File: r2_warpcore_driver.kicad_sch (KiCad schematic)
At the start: 1 part, among them U1 ESP32-S3-MINI-1

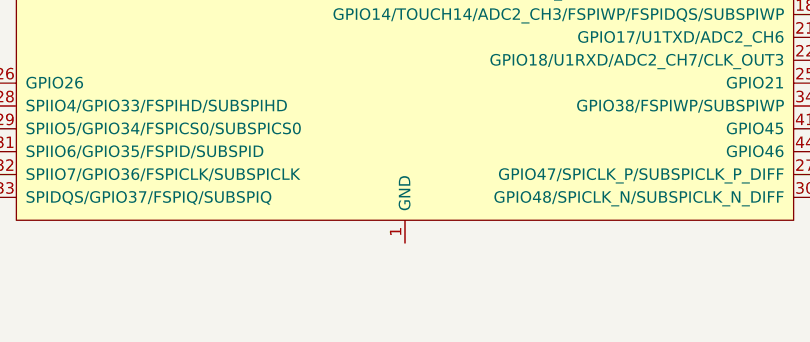
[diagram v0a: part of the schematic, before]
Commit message: Updates to build & adding hash insertion on PCB
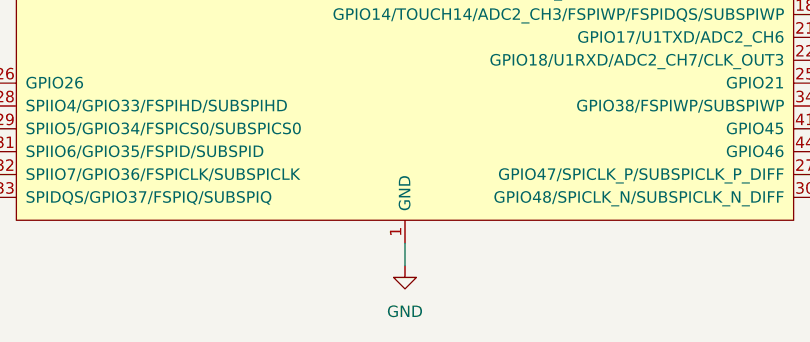
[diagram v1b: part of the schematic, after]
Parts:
- U1: JLCPCB (none) -> C3013941
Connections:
- net GND: now reaches U1.1 (GND), U1.2 (GND), U1.42 (GND), U1.43 (GND), U1.46 (GND), U1.47 (GND), U1.48 (GND), U1.49 (GND), U1.50 (GND), U1.51 (GND), U1.52 (GND), U1.53 (GND), U1.54 (GND), U1.55 (GND), U1.56 (GND), U1.57 (GND), U1.58 (GND), U1.59 (GND), U1.60 (GND), U1.61 (GND), U1.62 (GND), U1.63 (GND), U1.64 (GND), U1.65 (GND)
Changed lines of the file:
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@@
 (kicad_sch (version 20230121) (generator eeschema)
   (paper "A4")
+  (wire (pts (xy 91.44 110.49) (xy 91.44 113.03))
+    (stroke (width 0) (type default))
+  )
   (text "Needs:\n- drive motor control\n- pinout for ESP programming\n- support for pololu regulator to come from 12V down to 5V\n- support for driving 2 servos\n- support for switching on/off laser (7.5 v)\n- support for switching on/off fans (12v)\n- support for RGB LED\n- support for switching on / fog machine (5V 2A?)\n- support for switching on / off strobe (12V)\n- pinout for serial comms?\n- buttons for reset & boot\n- support to read linear actuator position"
     (at 214.63 40.64 0)
     (effects (font (size 1.27 1.27)) (justify left bottom))
+  )
+  (symbol (lib_id "power:GND") (at 91.44 113.03 0) (unit 1)
+    (in_bom yes) (on_board yes) (dnp no) (fields_autoplaced)
+    (property "Reference" "#PWR01" (at 91.44 119.38 0)
+      (effects (font (size 1.27 1.27)) hide)
+    )
+    (property "Value" "GND" (at 91.44 118.11 0)
+      (effects (font (size 1.27 1.27)))
+    )
+    (property "Footprint" "" (at 91.44 113.03 0)
+      (effects (font (size 1.27 1.27)) hide)
+    )
+    (property "Datasheet" "" (at 91.44 113.03 0)
+      (effects (font (size 1.27 1.27)) hide)
+    )
+    (pin "1")
+    (instances
+      (project "r2_warpcore_driver"
+        (path "/6d80d172-24e2-4eb2-ae83-4ad814eadecf"
+          (reference "#PWR01") (unit 1)
+        )
+      )
+    )
   )
   (symbol (lib_id "PCM_Espressif:ESP32-S3-MINI-1") (at 91.44 69.85 0) (unit 1)
@@
       (effects (font (size 1.27 1.27)) hide)
     )
+    (property "JLCPCB" "C3013941" (at 91.44 69.85 0)
+      (effects (font (size 1.27 1.27)) hide)
+    )

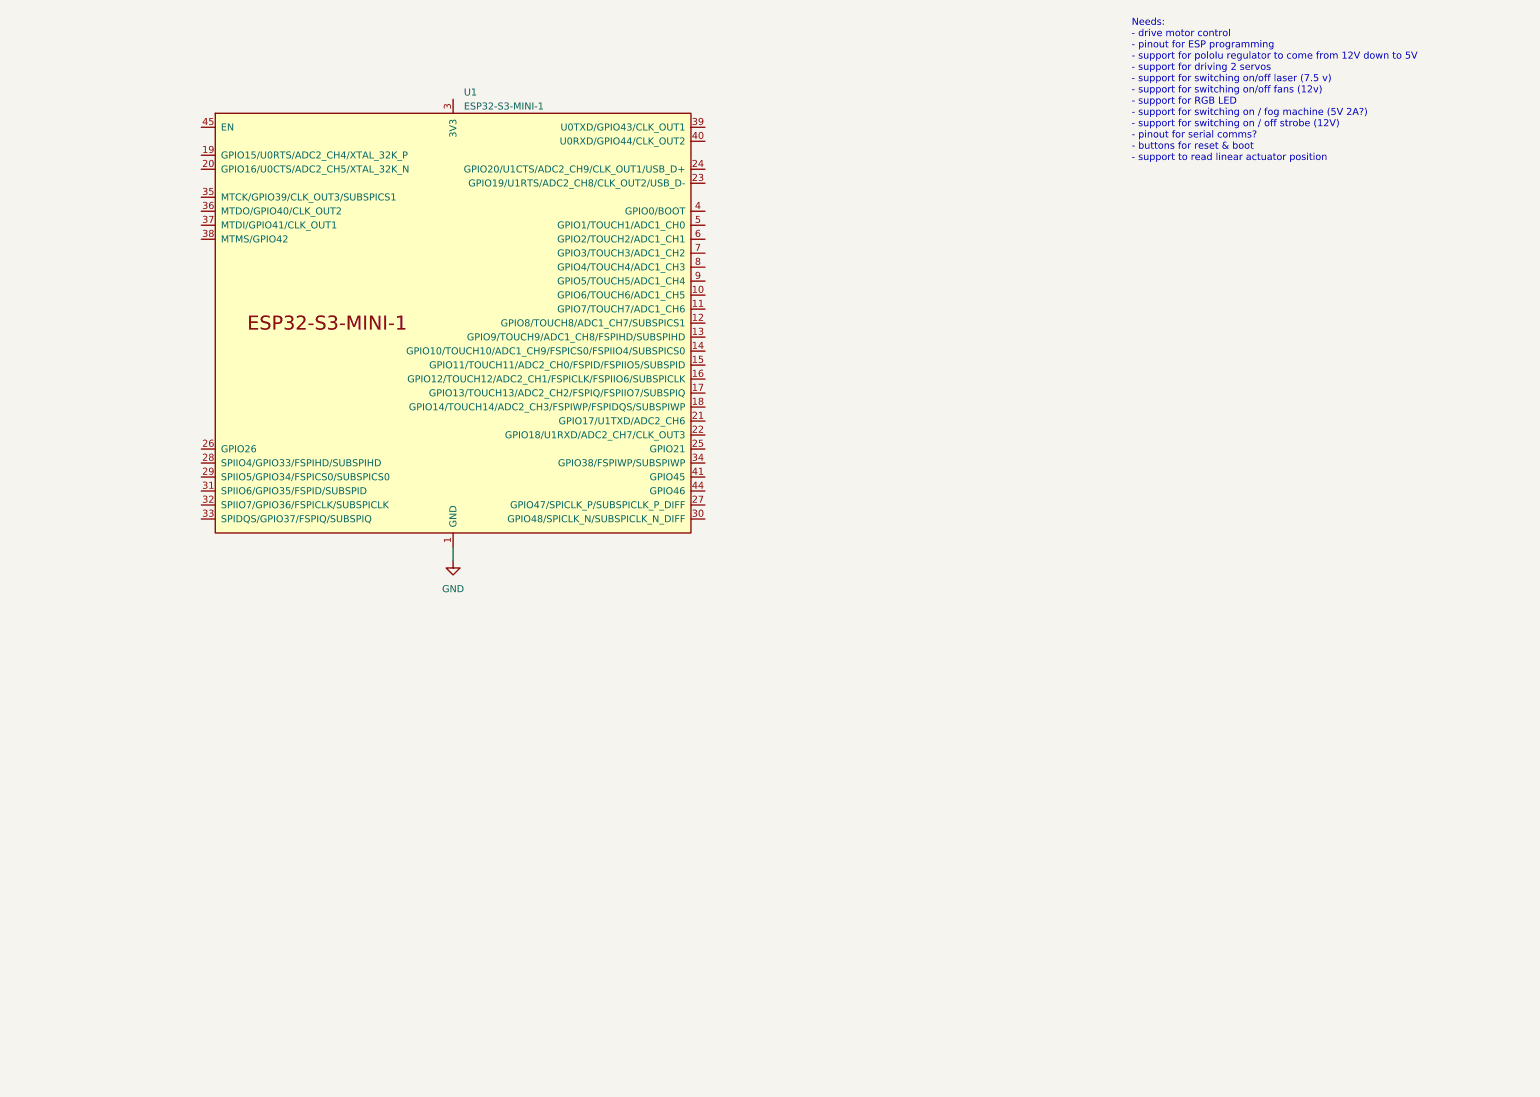
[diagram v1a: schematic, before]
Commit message: Updates with most of the layout completed. Still need to populate some JLCPCB parts and also need to specify the resistors for the LEDS. Should also review if we want to drive the LEDs directly from the MCU or if we want to put in some transistors to drive the LEDs from a higher voltage / current source.
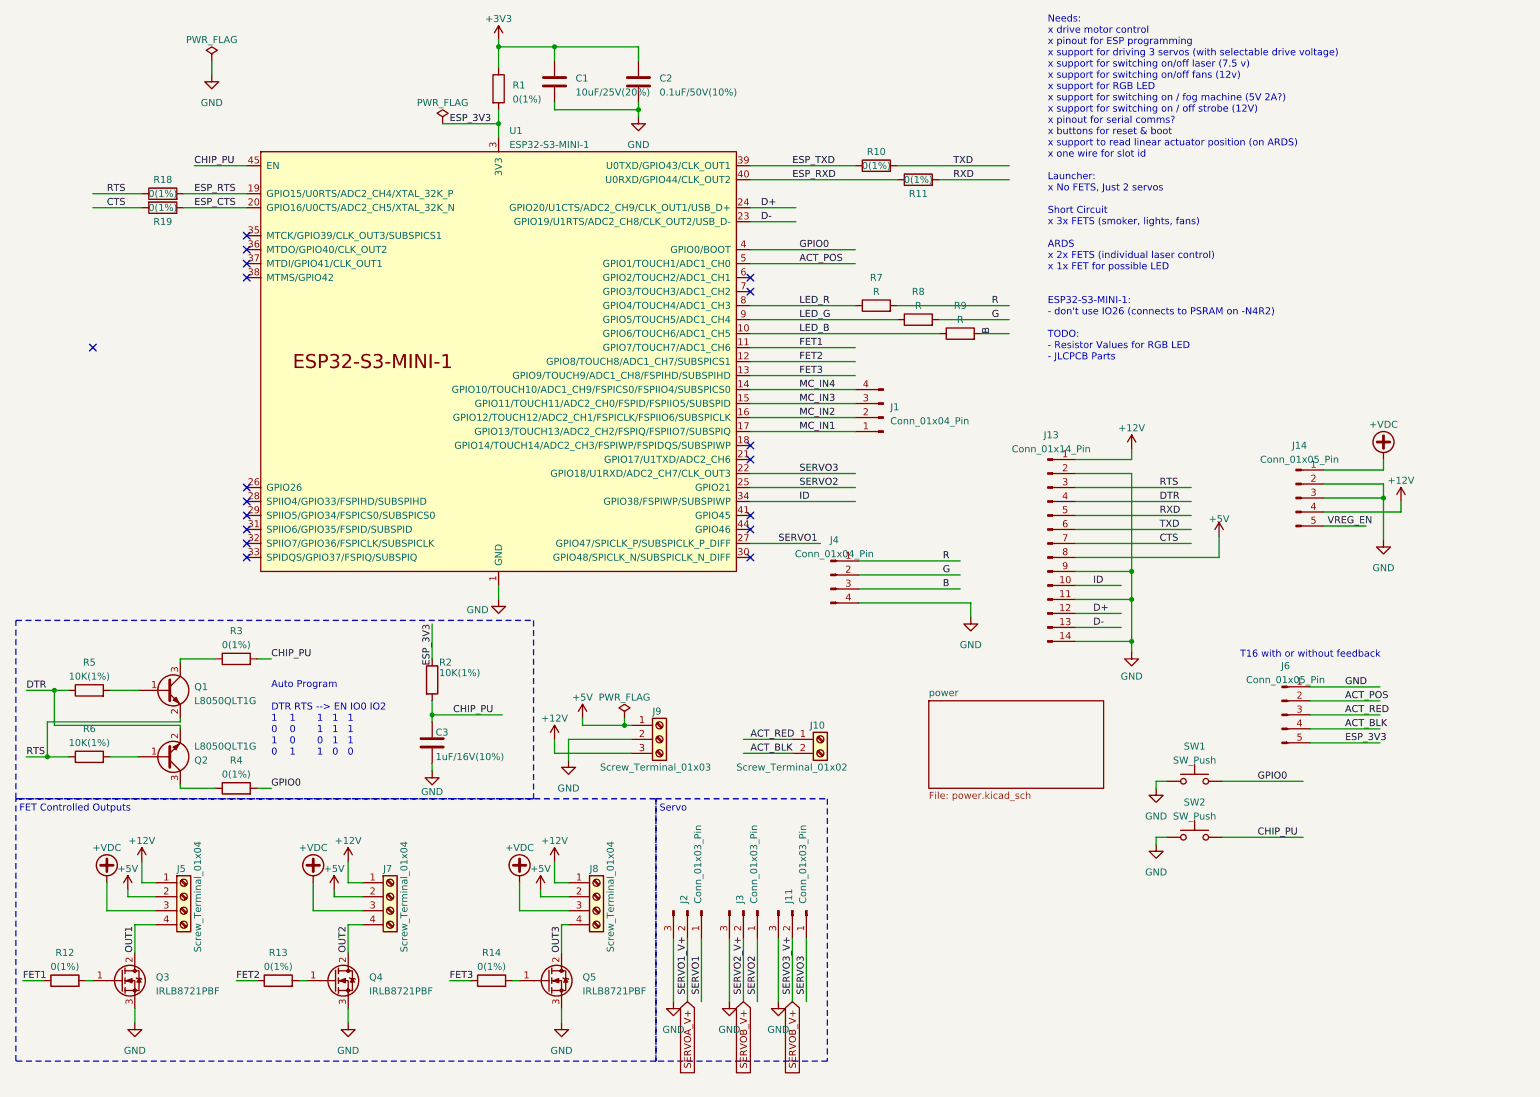
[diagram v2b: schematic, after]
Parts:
- added C1: 10uF/25V(20%), Capacitor_SMD:C_0402_1005Metric, symbol Device:C
- added C2: 0.1uF/50V(10%), Capacitor_SMD:C_0402_1005Metric, symbol Device:C
- added C3: 1uF/16V(10%), Capacitor_SMD:C_0402_1005Metric, symbol Device:C
- added J1: Conn_01x04_Pin, Connector_PinHeader_2.54mm:PinHeader_1x04_P2.54mm_Vertical, symbol Connector:Conn_01x04_Pin
- added J10: Screw_Terminal_01x02, Connector_Wire:SolderWire-0.75sqmm_1x02_P7mm_D1.25mm_OD3.5mm, symbol Connector:Screw_Terminal_01x02
- added J11, J2, J3: Conn_01x03_Pin, Connector_PinHeader_2.54mm:PinHeader_1x03_P2.54mm_Vertical, symbol Connector:Conn_01x03_Pin
- added J13: Conn_01x14_Pin, Connector_JST:JST_XH_B14B-XH-A_1x14_P2.50mm_Vertical, symbol Connector:Conn_01x14_Pin
- added J14, J6: Conn_01x05_Pin, Connector_PinHeader_2.54mm:PinHeader_1x05_P2.54mm_Vertical, symbol Connector:Conn_01x05_Pin
- added J4: Conn_01x04_Pin, Connector_JST:JST_XH_B4B-XH-A_1x04_P2.50mm_Vertical, symbol Connector:Conn_01x04_Pin
- added J5, J7, J8: Screw_Terminal_01x04, TerminalBlock_Phoenix:TerminalBlock_Phoenix_PT-1,5-4-3.5-H_1x04_P3.50mm_Horizontal, symbol Connector:Screw_Terminal_01x04
- added J9: Screw_Terminal_01x03, Connector_Wire:SolderWire-0.75sqmm_1x03_P7mm_D1.25mm_OD3.5mm, symbol Connector:Screw_Terminal_01x03
- added Q1, Q2: L8050QLT1G, Package_TO_SOT_SMD:SOT-23-3, symbol Device:Q_NPN_BEC
- added Q3, Q4, Q5: IRLB8721PBF, Package_TO_SOT_THT:TO-220-3_Vertical, symbol Transistor_FET:IRLB8721PBF
- added R1, R10, R11, R12, R13, R14, R18, R19, R3, R4: 0(1%), Resistor_SMD:R_0402_1005Metric, symbol Device:R
- added R2, R5, R6: 10K(1%), Resistor_SMD:R_0402_1005Metric, symbol Device:R
- added R7, R8, R9: R, Resistor_SMD:R_0402_1005Metric, symbol Device:R
- added SW1, SW2: SW_Push, Button_Switch_SMD:SW_Push_SPST_NO_Alps_SKRK, symbol Switch:SW_Push
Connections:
- net GND: now also C1.2, C2.2, C3.2, J11.3 (Pin_3), J13.11 (Pin_11), J13.14 (Pin_14), J13.2 (Pin_2), J13.9 (Pin_9), J14.2 (Pin_2), J14.3 (Pin_3), J2.3 (Pin_3), J3.3 (Pin_3), J4.4 (Pin_4), J6.1 (Pin_1), J9.2 (Pin_2), Q3.3 (S), Q4.3 (S), Q5.3 (S), SW1.1, SW2.1
- net LED_B: now reaches U1.10 (GPIO6/TOUCH6/ADC1_CH5)
- net LED_B: now also R9.1
- net FET1: now reaches U1.11 (GPIO7/TOUCH7/ADC1_CH6)
- net FET1: now also R12.1
- net FET2: now reaches U1.12 (GPIO8/TOUCH8/ADC1_CH7/SUBSPICS1)
- net FET2: now also R13.1
- net FET3: now reaches U1.13 (GPIO9/TOUCH9/ADC1_CH8/FSPIHD/SUBSPIHD)
- net FET3: now also R14.1
- net MC_IN4: now reaches U1.14 (GPIO10/TOUCH10/ADC1_CH9/FSPICS0/FSPIIO4/SUBSPICS0)
- net MC_IN4: now also J1.4 (Pin_4)
- net MC_IN3: now reaches U1.15 (GPIO11/TOUCH11/ADC2_CH0/FSPID/FSPIIO5/SUBSPID)
- net MC_IN3: now also J1.3 (Pin_3)
- net MC_IN2: now reaches U1.16 (GPIO12/TOUCH12/ADC2_CH1/FSPICLK/FSPIIO6/SUBSPICLK)
- net MC_IN2: now also J1.2 (Pin_2)
- net MC_IN1: now reaches U1.17 (GPIO13/TOUCH13/ADC2_CH2/FSPIQ/FSPIIO7/SUBSPIQ)
- net MC_IN1: now also J1.1 (Pin_1)
- net ESP_RTS: now reaches U1.19 (GPIO15/U0RTS/ADC2_CH4/XTAL_32K_P)
- net ESP_RTS: now also R18.2
- net ESP_CTS: now reaches U1.20 (GPIO16/U0CTS/ADC2_CH5/XTAL_32K_N)
- net ESP_CTS: now also R19.1
- net SERVO3: now reaches U1.22 (GPIO18/U1RXD/ADC2_CH7/CLK_OUT3)
- net SERVO3: now also J11.1 (Pin_1)
- net D-: now reaches U1.23 (GPIO19/U1RTS/ADC2_CH8/CLK_OUT2/USB_D-)
- net D-: now also J13.13 (Pin_13)
- net D+: now reaches U1.24 (GPIO20/U1CTS/ADC2_CH9/CLK_OUT1/USB_D+)
- net D+: now also J13.12 (Pin_12)
- net SERVO2: now reaches U1.25 (GPIO21)
- net SERVO2: now also J3.1 (Pin_1)
- net SERVO1: now reaches U1.27 (GPIO47/SPICLK_P/SUBSPICLK_P_DIFF)
- net SERVO1: now also J2.1 (Pin_1)
- net ESP_3V3: now reaches U1.3 (3V3)
- net ESP_3V3: now also J6.5 (Pin_5), R1.2, R2.1
- net ID: now reaches U1.34 (GPIO38/FSPIWP/SUBSPIWP)
- net ID: now also J13.10 (Pin_10)
- net ESP_TXD: now reaches U1.39 (U0TXD/GPIO43/CLK_OUT1)
- net ESP_TXD: now also R10.1
- net GPIO0: now reaches U1.4 (GPIO0/BOOT)
- net GPIO0: now also R4.2, SW1.2
- net ESP_RXD: now reaches U1.40 (U0RXD/GPIO44/CLK_OUT2)
- net ESP_RXD: now also R11.1
- net CHIP_PU: now reaches U1.45 (EN)
- net CHIP_PU: now also C3.1, R2.2, R3.2, SW2.2
- net ACT_POS: now reaches U1.5 (GPIO1/TOUCH1/ADC1_CH0)
- net ACT_POS: now also J6.2 (Pin_2)
- net LED_R: now reaches U1.8 (GPIO4/TOUCH4/ADC1_CH3)
- net LED_R: now also R7.1
- net LED_G: now reaches U1.9 (GPIO5/TOUCH5/ADC1_CH4)
- net LED_G: now also R8.1
- new net: Q1.1 (B), R5.2
- new net: Q1.3 (C), R3.1
- new net: Q4.1 (G), R13.2
- new net: Q2.1 (B), R6.2
- new net: Q2.3 (C), R4.1
- new net: Q5.1 (G), R14.2
- new net: Q3.1 (G), R12.2
- new net +12V: J13.1 (Pin_1), J14.4 (Pin_4), J5.1 (Pin_1), J7.1 (Pin_1), J8.1 (Pin_1), J9.3 (Pin_3)
- new net +3V3: C1.1, C2.1, R1.1
- new net +5V: J13.8 (Pin_8), J5.2 (Pin_2), J7.2 (Pin_2), J8.2 (Pin_2), J9.1 (Pin_1)
- new net +VDC: J14.1 (Pin_1), J5.3 (Pin_3), J7.3 (Pin_3), J8.3 (Pin_3)
- new net ACT_BLK: J10.2 (Pin_2), J6.4 (Pin_4)
- new net ACT_RED: J10.1 (Pin_1), J6.3 (Pin_3)
- new net B: J4.3 (Pin_3), R9.2
- new net CTS: J13.7 (Pin_7), R19.2
- new net DTR: J13.4 (Pin_4), Q2.2 (E), R5.1
- new net G: J4.2 (Pin_2), R8.2
- new net OUT1: J5.4 (Pin_4), Q3.2 (D)
- new net OUT2: J7.4 (Pin_4), Q4.2 (D)
- new net OUT3: J8.4 (Pin_4), Q5.2 (D)
- new net R: J4.1 (Pin_1), R7.2
- new net RTS: J13.3 (Pin_3), Q1.2 (E), R18.1, R6.1
- new net RXD: J13.5 (Pin_5), R11.2
- new net SERVOA_V+: J2.2 (Pin_2)
- new net SERVOB_V+: J11.2 (Pin_2), J3.2 (Pin_2)
- new net TXD: J13.6 (Pin_6), R10.2
- new net VREG_EN: J14.5 (Pin_5)
- no-connect marks 0 -> 18
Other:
- added sheet power (power.kicad_sch)
- note added: "Auto Program DTR RTS --> EN IO0 IO2 1 1 1 1 1 0 0 1 1 1 1 0 0 1 1 0 1 1 0 0"
- note added: "FET Controlled Outputs"
- note added: "Needs: x drive motor control x pinout for ESP programming x support for driving 3 servos (with selectable drive voltage) x support for switching on/off laser (7.5 v) x support for switching on/off fans (12v) x support for RGB LED x support for switching on / fog machine (5V 2A?) x support for switching on / off strobe (12V) x pinout for serial comms? x buttons for reset & boot x support to read l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"
- note added: "Servo"
- note added: "T16 with or without feedback"
- note removed: "Needs: - drive motor control - pinout for ESP programming - support for pololu regulator to come from 12V down to 5V - support for driving 2 servos - support for switching on/off laser (7.5 v) - support for switching on/off fans (12v) - support for RGB LED - support for switching on / fog machine (5V 2A?) - support for switching on / off strobe (12V) - pinout for serial comms? - buttons for reset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"
- moved on the sheet: U1

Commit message: Adding URL & git hash placeholder information in as well as a note for more todo
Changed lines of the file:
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@@
     (effects (font (size 1.27 1.27)) (justify left bottom))
   )
-  (text "Needs:\nx drive motor control\nx pinout for ESP programming\nx support for driving 3 servos (with selectable drive voltage)\nx support for switching on/off laser (7.5 v)\nx support for switching on/off fans (12v)\nx support for RGB LED\nx support for switching on / fog machine (5V 2A?)\nx support for switching on / off strobe (12V)\nx pinout for serial comms?\nx buttons for reset & boot\nx support to read linear actuator position (on ARDS)\nx one wire for slot id\n\nLauncher:\nx No FETS, Just 2 servos\n\nShort Circuit\nx 3x FETS (smoker, lights, fans)\n\nARDS\nx 2x FETS (individual laser control)\nx 1x FET for possible LED\n\n\nESP32-S3-MINI-1:\n- don't use IO26 (connects to PSRAM on -N4R2)\n\nTODO:\n- Resistor Values for RGB LED\n- JLCPCB Parts"
-    (at 199.39 76.835 0)
+  (text "Needs:\nx drive motor control\nx pinout for ESP programming\nx support for driving 3 servos (with selectable drive voltage)\nx support for switching on/off laser (7.5 v)\nx support for switching on/off fans (12v)\nx support for RGB LED\nx support for switching on / fog machine (5V 2A?)\nx support for switching on / off strobe (12V)\nx pinout for serial comms?\nx buttons for reset & boot\nx support to read linear actuator position (on ARDS)\nx one wire for slot id\n\nLauncher:\nx No FETS, Just 2 servos\n\nShort Circuit\nx 3x FETS (smoker, lights, fans)\n\nARDS\nx 2x FETS (individual laser control)\nx 1x FET for possible LED\n\n\nESP32-S3-MINI-1:\n- don't use IO26 (connects to PSRAM on -N4R2)\n\nTODO:\n- Resistor Values for RGB LED\n- JLCPCB Parts\n- USB diodes?"
+    (at 203.2 81.915 0)
     (effects (font (size 1.27 1.27)) (justify left bottom))
   )
